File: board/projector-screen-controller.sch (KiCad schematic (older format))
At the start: 8 parts, among them J2 MSTBVA-3-G, J3 RS232 #1, J4 RS232 #2, J5 Buttons, J6 MSTBVA-6-G

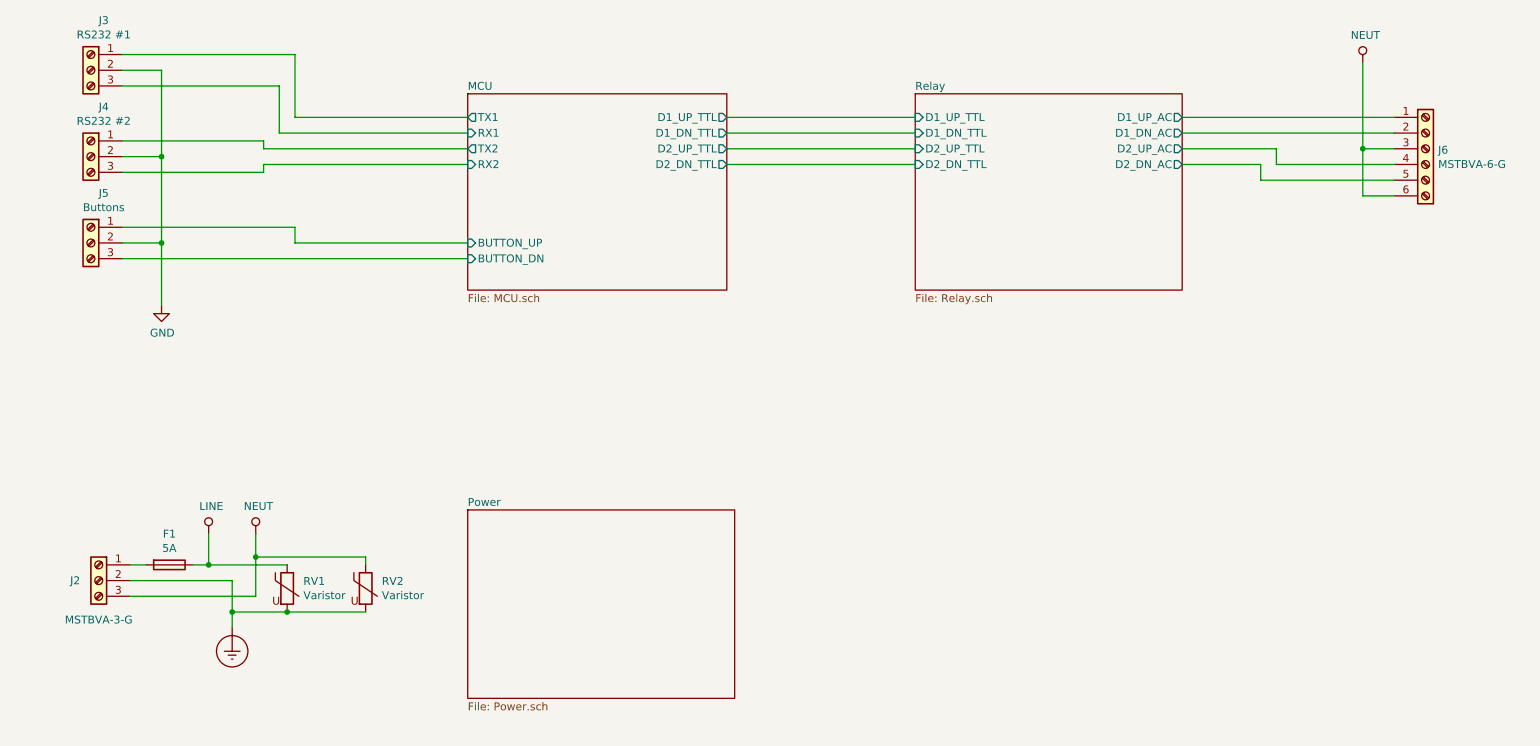
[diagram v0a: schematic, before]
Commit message: Add button 2, LEDs, TVS diode
* Add button 2; rewire to match the prototype
* Add a TVS diode across the 12V rail; value TBD
* Rework power nets into the power sheet; don't use the globals
  inside the sheet, expose the rails as pins.
* Move power protection inside the power sheet.
* Add power LEDs
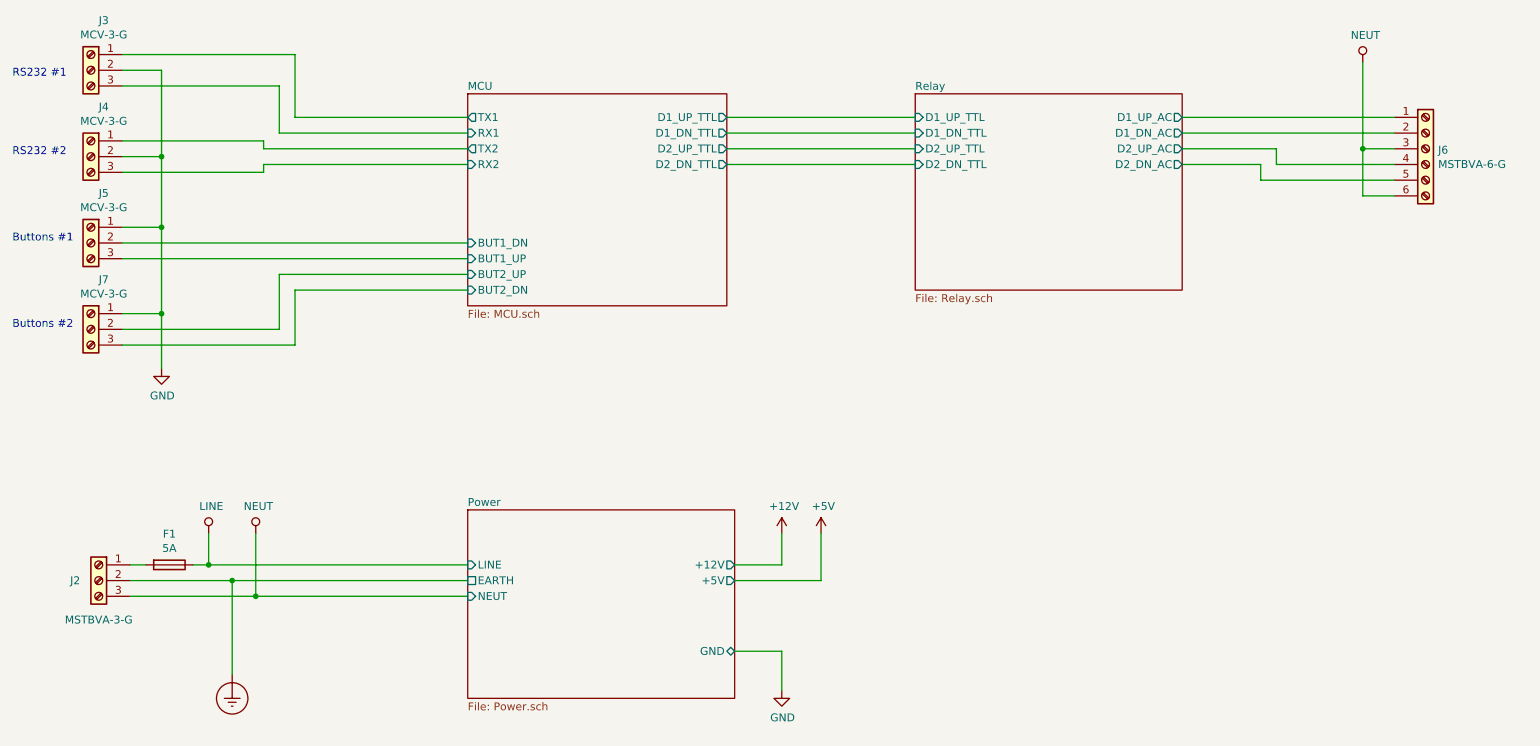
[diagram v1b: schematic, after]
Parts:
- removed RV1, RV2: Varistor, Varistors:RV_Disc_D15.5_W7.2_P7.5, symbol Device:Varistor
- added J7: MCV-3-G, Connectors_Phoenix:PhoenixContact_MCV-G_03x3.50mm_Vertical, symbol Connector:Screw_Terminal_01x03
- J3: value RS232 #1 -> MCV-3-G
- J4: value RS232 #2 -> MCV-3-G
- J5: value Buttons -> MCV-3-G
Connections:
- net MCU/BUTTON_UP is gone; now on net GND: J5.1 (Pin_1)
- net GND: now also J7.1 (Pin_1); no longer J5.2 (Pin_2)
- net MCU/BUTTON_DN renamed MCU/BUT1_UP
- new net MCU/BUT1_DN: J5.2 (Pin_2)
- new net MCU/BUT2_DN: J7.3 (Pin_3)
- new net MCU/BUT2_UP: J7.2 (Pin_2)
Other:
- note added: "Buttons #1"
- note added: "Buttons #2"
- note added: "RS232 #1"
- note added: "RS232 #2"
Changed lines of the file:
@@
 Sheet 1 4
 Title "Projector Screen Controller"
-Date ""
+Date "2019-08-31"
 Rev "0.1"
 Comp "Chris Luke"
-Comment1 ""
+Comment1 "https://github.com/flirbleoss/projector-screen-controller"
 Comment2 ""
 Comment3 ""
@@
 $EndDescr
 $Sheet
-S 3750 2200 1650 1250
+S 3750 2200 1650 1350
 U 5D6871CF
 F0 "MCU" 50
@@
 F8 "D2_UP_TTL" O R 5400 2550 50
 F9 "D2_DN_TTL" O R 5400 2650 50
-F10 "BUTTON_UP" I L 3750 3150 50
-F11 "BUTTON_DN" I L 3750 3250 50
+F10 "BUT1_UP" I L 3750 3250 50
+F11 "BUT1_DN" I L 3750 3150 50
+F12 "BUT2_UP" I L 3750 3350 50
+F13 "BUT2_DN" I L 3750 3450 50
 $EndSheet
 $Sheet
@@
 F0 "Power" 50
 F1 "Power.sch" 50
+F2 "LINE" I L 3750 5200 50
+F3 "NEUT" I L 3750 5400 50
+F4 "+12V" O R 5450 5200 50
+F5 "+5V" O R 5450 5300 50
+F6 "GND" B R 5450 5750 50
+F7 "EARTH" U L 3750 5300 50
 $EndSheet
 $Comp
@@
 L power:Earth_Protective #PWR0103
 U 1 1 5D6FA28C
-P 2250 5600
-F 0 "#PWR0103" H 2500 5350 50  0001 C CNN
-F 1 "Earth_Protective" H 2700 5450 50  0001 C CNN
-F 2 "" H 2250 5500 50  0001 C CNN
-F 3 "~" H 2250 5500 50  0001 C CNN
-	1    2250 5600
+P 2250 5900
+F 0 "#PWR0103" H 2500 5650 50  0001 C CNN
+F 1 "Earth_Protective" H 2700 5750 50  0001 C CNN
+F 2 "" H 2250 5800 50  0001 C CNN
+F 3 "~" H 2250 5800 50  0001 C CNN
+	1    2250 5900
 	1    0    0    -1
 $EndComp
@@
 	1600 5400 2400 5400
 Wire Wire Line
-	2400 5400 2400 5150
-Wire Wire Line
 	5400 2350 6600 2350
 Wire Wire Line
@@
 P 1350 2050
 F 0 "J3" H 1268 2367 50  0000 C CNN
-F 1 "RS232 #1" H 1268 2276 50  0000 C CNN
+F 1 "MCV-3-G" H 1268 2276 50  0000 C CNN
 F 2 "Connectors_Phoenix:PhoenixContact_MCV-G_03x3.50mm_Vertical" H 1350 2050 50  0001 C CNN
 F 3 "~" H 1350 2050 50  0001 C CNN
@@
 P 1350 2600
 F 0 "J4" H 1268 2917 50  0000 C CNN
-F 1 "RS232 #2" H 1268 2826 50  0000 C CNN
+F 1 "MCV-3-G" H 1268 2826 50  0000 C CNN
 F 2 "Connectors_Phoenix:PhoenixContact_MCV-G_03x3.50mm_Vertical" H 1350 2600 50  0001 C CNN
 F 3 "~" H 1350 2600 50  0001 C CNN
@@
 P 1350 3150
 F 0 "J5" H 1268 3467 50  0000 C CNN
-F 1 "Buttons" H 1268 3376 50  0000 C CNN
+F 1 "MCV-3-G" H 1268 3376 50  0000 C CNN
 F 2 "Connectors_Phoenix:PhoenixContact_MCV-G_03x3.50mm_Vertical" H 1350 3150 50  0001 C CNN
 F 3 "~" H 1350 3150 50  0001 C CNN
@@
 	-1   0    0    -1
 $EndComp
-Wire Wire Line
-	1550 3050 2650 3050
-Wire Wire Line
-	2650 3050 2650 3150
-Wire Wire Line
-	2650 3150 3750 3150
-Wire Wire Line
-	1550 3250 3750 3250
 $Comp
 L power:GND #PWR013
 U 1 1 5D70709B
-P 1800 3550
-F 0 "#PWR013" H 1800 3300 50  0001 C CNN
-F 1 "GND" H 1805 3377 50  0000 C CNN
-F 2 "" H 1800 3550 50  0001 C CNN
-F 3 "" H 1800 3550 50  0001 C CNN
-	1    1800 3550
-	1    0    0    -1
-$EndComp
-Wire Wire Line
-	1550 3150 1800 3150
-Wire Wire Line
-	1800 3150 1800 3550
+P 1800 3950
+F 0 "#PWR013" H 1800 3700 50  0001 C CNN
+F 1 "GND" H 1805 3777 50  0000 C CNN
+F 2 "" H 1800 3950 50  0001 C CNN
+F 3 "" H 1800 3950 50  0001 C CNN
+	1    1800 3950
+	1    0    0    -1
+$EndComp
 Wire Wire Line
 	1550 2600 1800 2600
-Wire Wire Line
-	1800 2600 1800 3150
-Connection ~ 1800 3150
 Wire Wire Line
 	1550 2050 1800 2050
@@
 Wire Wire Line
 	2000 5200 2100 5200
-$Comp
-L Device:Varistor RV1
-U 1 1 5D769A2F
-P 2600 5350
-F 0 "RV1" H 2703 5396 50  0000 L CNN
-F 1 "Varistor" H 2703 5305 50  0000 L CNN
-F 2 "Varistors:RV_Disc_D15.5_W7.2_P7.5" V 2530 5350 50  0001 C CNN
-F 3 "~" H 2600 5350 50  0001 C CNN
-	1    2600 5350
-	1    0    0    -1
-$EndComp
-Wire Wire Line
-	2250 5300 2250 5500
-Wire Wire Line
-	2600 5500 2250 5500
-Connection ~ 2250 5500
-Wire Wire Line
-	2250 5500 2250 5600
-Wire Wire Line
-	2100 5200 2600 5200
 Connection ~ 2100 5200
-$Comp
-L Device:Varistor RV2
-U 1 1 5D76EEBE
-P 3100 5350
-F 0 "RV2" H 3203 5396 50  0000 L CNN
-F 1 "Varistor" H 3203 5305 50  0000 L CNN
-F 2 "Varistors:RV_Disc_D15.5_W7.2_P7.5" V 3030 5350 50  0001 C CNN
-F 3 "~" H 3100 5350 50  0001 C CNN
-	1    3100 5350
-	1    0    0    -1
-$EndComp
-Wire Wire Line
-	3100 5500 2600 5500
-Connection ~ 2600 5500
-Wire Wire Line
-	3100 5200 3100 5150
-Wire Wire Line
-	3100 5150 2400 5150
-Connection ~ 2400 5150
-Wire Wire Line
-	2400 5150 2400 5000
+Text Notes 850  2100 0    50   ~ 0
+RS232 #1
+Text Notes 850  2600 0    50   ~ 0
+RS232 #2
+Text Notes 850  3150 0    50   ~ 0
+Buttons #1
+$Comp
+L Connector:Screw_Terminal_01x03 J7
+U 1 1 5D6D108D
+P 1350 3700
+F 0 "J7" H 1268 4017 50  0000 C CNN
+F 1 "MCV-3-G" H 1268 3926 50  0000 C CNN
+F 2 "Connectors_Phoenix:PhoenixContact_MCV-G_03x3.50mm_Vertical" H 1350 3700 50  0001 C CNN
+F 3 "~" H 1350 3700 50  0001 C CNN
+	1    1350 3700
+	-1   0    0    -1
+$EndComp
+Wire Wire Line
+	1800 2600 1800 3050
+Wire Wire Line
+	1550 3050 1800 3050
+Connection ~ 1800 3050
+Wire Wire Line
+	1550 3150 3750 3150
+Wire Wire Line
+	1550 3250 3750 3250
+Wire Wire Line
+	1550 3600 1800 3600
+Wire Wire Line
+	1800 3050 1800 3600
+Connection ~ 1800 3600
+Wire Wire Line
+	1800 3600 1800 3950
+Wire Wire Line
+	3750 3450 2650 3450
+Wire Wire Line
+	2650 3450 2650 3800
+Wire Wire Line
+	2650 3800 1550 3800
+Wire Wire Line
+	3750 3350 2550 3350
+Wire Wire Line
+	2550 3350 2550 3700
+Wire Wire Line
+	2550 3700 1550 3700
+Text Notes 850  3700 0    50   ~ 0
+Buttons #2
+Wire Wire Line
+	2400 5000 2400 5400
+Connection ~ 2400 5400
+$Comp
+L power:GND #PWR0104
+U 1 1 5D6F4A37
+P 5750 6000
+F 0 "#PWR0104" H 5750 5750 50  0001 C CNN
+F 1 "GND" H 5755 5827 50  0000 C CNN
+F 2 "" H 5750 6000 50  0001 C CNN
+F 3 "" H 5750 6000 50  0001 C CNN
+	1    5750 6000
+	1    0    0    -1
+$EndComp
+Wire Wire Line
+	5450 5750 5750 5750
+Wire Wire Line
+	5750 5750 5750 6000
+$Comp
+L power:+12V #PWR0105
+U 1 1 5D6F727B
+P 5750 5000
+F 0 "#PWR0105" H 5750 4850 50  0001 C CNN
+F 1 "+12V" H 5765 5173 50  0000 C CNN
+F 2 "" H 5750 5000 50  0001 C CNN
+F 3 "" H 5750 5000 50  0001 C CNN
+	1    5750 5000
+	1    0    0    -1
+$EndComp
+$Comp
+L power:+5V #PWR0109
+U 1 1 5D6F7C73
+P 6000 5000
+F 0 "#PWR0109" H 6000 4850 50  0001 C CNN
+F 1 "+5V" H 6015 5173 50  0000 C CNN
+F 2 "" H 6000 5000 50  0001 C CNN
+F 3 "" H 6000 5000 50  0001 C CNN
+	1    6000 5000
+	1    0    0    -1
+$EndComp
+Wire Wire Line
+	5750 5000 5750 5200
+Wire Wire Line
+	5750 5200 5450 5200
+Wire Wire Line
+	6000 5000 6000 5300
+Wire Wire Line
+	6000 5300 5450 5300
+Wire Wire Line
+	2100 5200 3750 5200
+Wire Wire Line
+	2400 5400 3750 5400
+Wire Wire Line
+	2250 5300 2250 5900
+Wire Wire Line
+	2250 5300 3750 5300
+Connection ~ 2250 5300
 $EndSCHEMATC

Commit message: Update fuse footprint, add more 3d models, update TODO
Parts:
- F1: footprint Fuse_Holders_and_Fuses:Fuseholder5x20_horiz_open_universal_Type-III -> Fuse_Holders_and_Fuses:Fuseholder5x20_horiz_open_inline_Type-I
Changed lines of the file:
@@
 F 0 "F1" V 1653 5200 50  0000 C CNN
 F 1 "5A" V 1744 5200 50  0000 C CNN
-F 2 "Fuse_Holders_and_Fuses:Fuseholder5x20_horiz_open_universal_Type-III" V 1780 5200 50  0001 C CNN
+F 2 "Fuse_Holders_and_Fuses:Fuseholder5x20_horiz_open_inline_Type-I" V 1780 5200 50  0001 C CNN
 F 3 "~" H 1850 5200 50  0001 C CNN
 	1    1850 5200

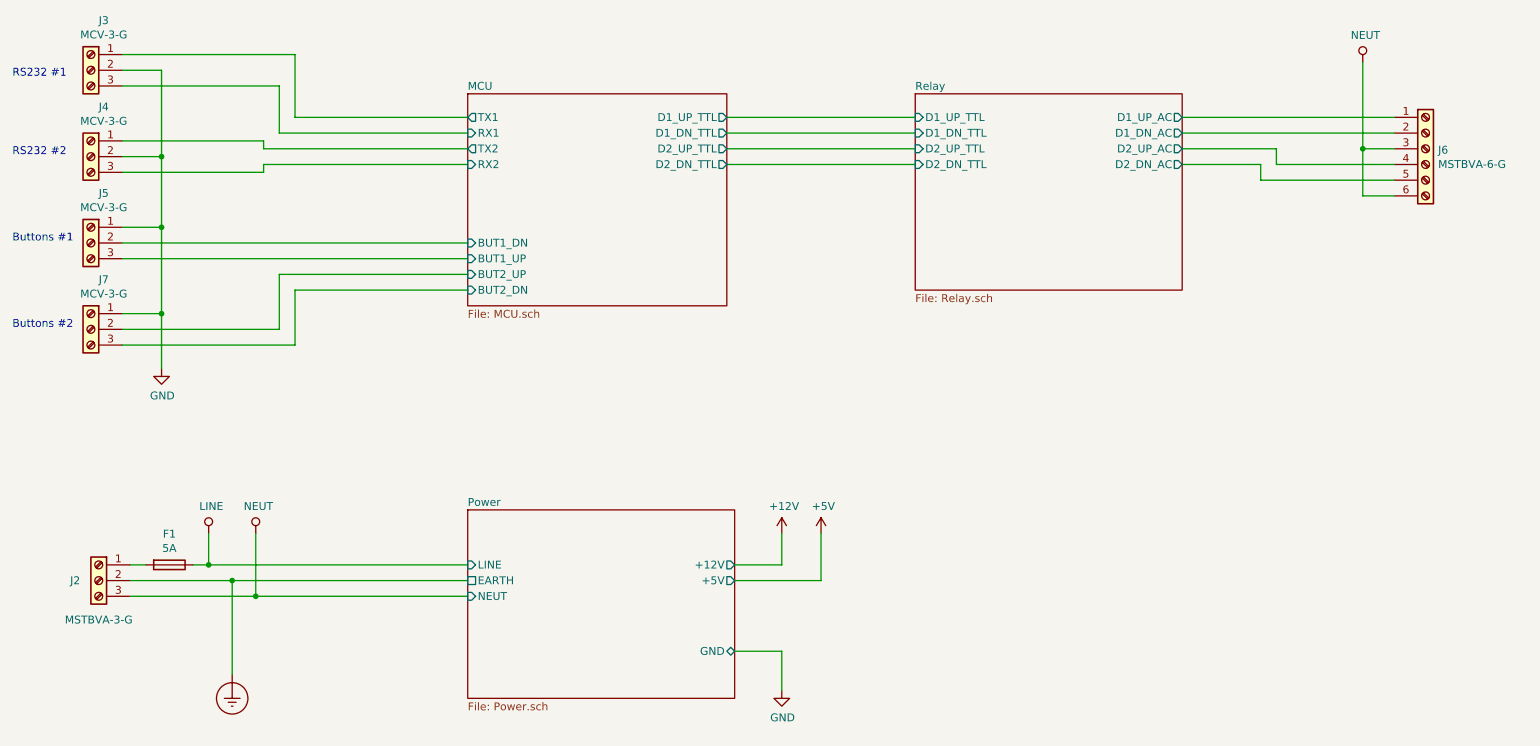
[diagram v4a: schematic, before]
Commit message: Split the 5v and 12v ground paths
* To control the return path for (noisy) relay current, split the grounds for
  the 12v and 5v sections.
* The grounds are joined by bridges (solder pads) placed adjacent to the 5v
  regulator, on both layers.
* The gound plane is split in two; conveniently the 12v vs 5v components were
  already well placed to make this straightforward.
* 12v power LED uses the 5v ground to simplify routing.
* Add dummy power flags for ERC
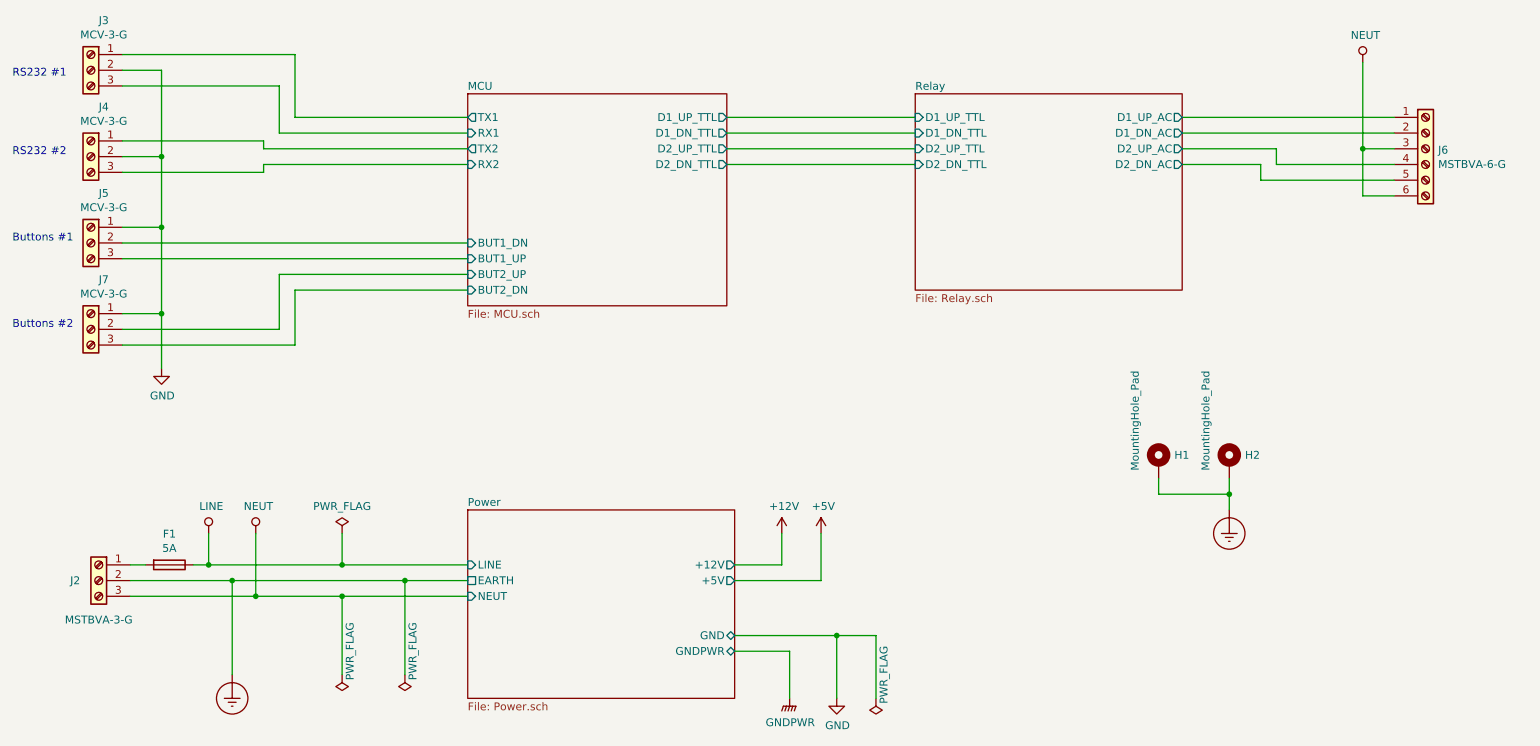
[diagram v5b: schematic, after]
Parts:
- added H1, H2: MountingHole_Pad, Mounting_Holes:MountingHole_3.7mm_Pad_Via, symbol Mechanical:MountingHole_Pad
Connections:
- net Earth_Protective: now also H1.1, H2.1
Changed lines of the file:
@@
 Sheet 1 4
 Title "Projector Screen Controller"
-Date "2019-09-02"
+Date "2019-09-07"
 Rev "0.2"
 Comp "Flirble Open Source"
@@
 F4 "+12V" O R 5450 5200 50
 F5 "+5V" O R 5450 5300 50
-F6 "GND" B R 5450 5750 50
+F6 "GND" B R 5450 5650 50
 F7 "EARTH" U L 3750 5300 50
+F8 "GNDPWR" B R 5450 5750 50
 $EndSheet
 $Comp
@@
 L power:GND #PWR0104
 U 1 1 5D6F4A37
-P 5750 6000
-F 0 "#PWR0104" H 5750 5750 50  0001 C CNN
-F 1 "GND" H 5755 5827 50  0000 C CNN
-F 2 "" H 5750 6000 50  0001 C CNN
-F 3 "" H 5750 6000 50  0001 C CNN
-	1    5750 6000
-	1    0    0    -1
-$EndComp
-Wire Wire Line
-	5450 5750 5750 5750
-Wire Wire Line
-	5750 5750 5750 6000
+P 6100 6050
+F 0 "#PWR0104" H 6100 5800 50  0001 C CNN
+F 1 "GND" H 6105 5877 50  0000 C CNN
+F 2 "" H 6100 6050 50  0001 C CNN
+F 3 "" H 6100 6050 50  0001 C CNN
+	1    6100 6050
+	1    0    0    -1
+$EndComp
 $Comp
 L power:+12V #PWR0105
@@
 	6000 5300 5450 5300
 Wire Wire Line
-	2100 5200 3750 5200
-Wire Wire Line
-	2400 5400 3750 5400
+	2100 5200 2950 5200
+Wire Wire Line
+	2400 5400 2950 5400
 Wire Wire Line
 	2250 5300 2250 5900
 Wire Wire Line
-	2250 5300 3750 5300
+	2250 5300 3350 5300
 Connection ~ 2250 5300
+$Comp
+L Mechanical:MountingHole_Pad H2
+U 1 1 5D799A5F
+P 8600 4550
+F 0 "H2" H 8700 4599 50  0000 L CNN
+F 1 "MountingHole_Pad" V 8450 4500 50  0000 L CNN
+F 2 "Mounting_Holes:MountingHole_3.7mm_Pad_Via" H 8600 4550 50  0001 C CNN
+F 3 "~" H 8600 4550 50  0001 C CNN
+	1    8600 4550
+	1    0    0    -1
+$EndComp
+$Comp
+L Mechanical:MountingHole_Pad H1
+U 1 1 5D79A14C
+P 8150 4550
+F 0 "H1" H 8250 4599 50  0000 L CNN
+F 1 "MountingHole_Pad" V 8000 4500 50  0000 L CNN
+F 2 "Mounting_Holes:MountingHole_3.7mm_Pad_Via" H 8150 4550 50  0001 C CNN
+F 3 "~" H 8150 4550 50  0001 C CNN
+	1    8150 4550
+	1    0    0    -1
+$EndComp
+$Comp
+L power:Earth_Protective #PWR010
+U 1 1 5D79B95E
+P 8600 4850
+F 0 "#PWR010" H 8850 4600 50  0001 C CNN
+F 1 "Earth_Protective" H 9050 4700 50  0001 C CNN
+F 2 "" H 8600 4750 50  0001 C CNN
+F 3 "~" H 8600 4750 50  0001 C CNN
+	1    8600 4850
+	1    0    0    -1
+$EndComp
+Wire Wire Line
+	8600 4650 8600 4750
+Wire Wire Line
+	8150 4650 8150 4750
+Wire Wire Line
+	8150 4750 8600 4750
+Connection ~ 8600 4750
+Wire Wire Line
+	8600 4750 8600 4850
+$Comp
+L power:GNDPWR #PWR0106
+U 1 1 5D7560D9
+P 5800 6050
+F 0 "#PWR0106" H 5800 5850 50  0001 C CNN
+F 1 "GNDPWR" H 5804 5896 50  0000 C CNN
+F 2 "" H 5800 6000 50  0001 C CNN
+F 3 "" H 5800 6000 50  0001 C CNN
+	1    5800 6050
+	1    0    0    -1
+$EndComp
+Wire Wire Line
+	5450 5650 6100 5650
+Wire Wire Line
+	6100 5650 6100 6050
+Wire Wire Line
+	5450 5750 5800 5750
+Wire Wire Line
+	5800 5750 5800 6050
+$Comp
+L power:PWR_FLAG #FLG0101
+U 1 1 5D7958CA
+P 2950 5000
+F 0 "#FLG0101" H 2950 5075 50  0001 C CNN
+F 1 "PWR_FLAG" H 2950 5173 50  0000 C CNN
+F 2 "" H 2950 5000 50  0001 C CNN
+F 3 "~" H 2950 5000 50  0001 C CNN
+	1    2950 5000
+	1    0    0    -1
+$EndComp
+$Comp
+L power:PWR_FLAG #FLG0102
+U 1 1 5D796A16
+P 2950 5900
+F 0 "#FLG0102" H 2950 5975 50  0001 C CNN
+F 1 "PWR_FLAG" V 2900 5750 50  0000 C CNN
+F 2 "" H 2950 5900 50  0001 C CNN
+F 3 "~" H 2950 5900 50  0001 C CNN
+	1    2950 5900
+	-1   0    0    1
+$EndComp
+$Comp
+L power:PWR_FLAG #FLG0103
+U 1 1 5D797EE8
+P 3350 5900
+F 0 "#FLG0103" H 3350 5975 50  0001 C CNN
+F 1 "PWR_FLAG" V 3300 5750 50  0000 C CNN
+F 2 "" H 3350 5900 50  0001 C CNN
+F 3 "~" H 3350 5900 50  0001 C CNN
+	1    3350 5900
+	-1   0    0    1
+$EndComp
+Wire Wire Line
+	2950 5000 2950 5200
+Connection ~ 2950 5200
+Wire Wire Line
+	2950 5200 3750 5200
+Wire Wire Line
+	2950 5400 2950 5900
+Connection ~ 2950 5400
+Wire Wire Line
+	2950 5400 3750 5400
+Wire Wire Line
+	3350 5300 3350 5900
+Connection ~ 3350 5300
+Wire Wire Line
+	3350 5300 3750 5300
+$Comp
+L power:PWR_FLAG #FLG0104
+U 1 1 5D79E448
+P 6350 6050
+F 0 "#FLG0104" H 6350 6125 50  0001 C CNN
+F 1 "PWR_FLAG" V 6300 5900 50  0000 C CNN
+F 2 "" H 6350 6050 50  0001 C CNN
+F 3 "~" H 6350 6050 50  0001 C CNN
+	1    6350 6050
+	-1   0    0    1
+$EndComp
+Wire Wire Line
+	6100 5650 6350 5650
+Wire Wire Line
+	6350 5650 6350 6050
+Connection ~ 6100 5650
 $EndSCHEMATC
